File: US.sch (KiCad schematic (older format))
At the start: 1 part, among them J10 Conn_01x04

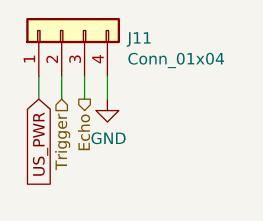
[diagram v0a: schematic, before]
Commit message: PCB routed, no errors but still a few tracks too close
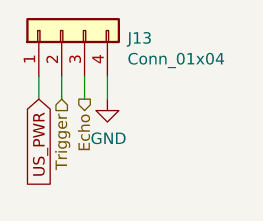
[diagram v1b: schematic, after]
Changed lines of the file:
@@
 AR Path="/5BC05284/5BC053B5" Ref="J12"  Part="1"
 AR Path="/5BC05291/5BC053B5" Ref="J13"  Part="1"
-F 0 "J11" V 3966 2262 50  0000 R CNN
+F 0 "J13" V 3966 2262 50  0000 R CNN
 F 1 "Conn_01x04" V 3875 2262 50  0000 R CNN
 F 2 "Connector_JST:JST_PH_B4B-PH-K_1x04_P2.00mm_Vertical" H 4000 2550 50  0001 C CNN
@@
 AR Path="/5BC05284/5BC072A4" Ref="#PWR053"  Part="1"
 AR Path="/5BC05291/5BC072A4" Ref="#PWR054"  Part="1"
-F 0 "#PWR052" H 4200 2600 50  0001 C CNN
+F 0 "#PWR054" H 4200 2600 50  0001 C CNN
 F 1 "GND" H 4205 2677 50  0000 C CNN
 F 2 "" H 4200 2850 50  0001 C CNN

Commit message: Corrected, routing redone
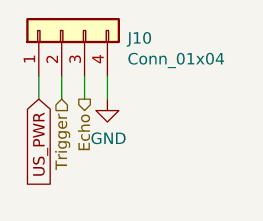
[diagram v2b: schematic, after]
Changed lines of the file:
@@
 $Descr A4 11693 8268
 encoding utf-8
-Sheet 12 19
+Sheet 15 19
 Title ""
 Date ""
@@
 AR Path="/5BC05284/5BC053B5" Ref="J12"  Part="1"
 AR Path="/5BC05291/5BC053B5" Ref="J13"  Part="1"
-F 0 "J13" V 3966 2262 50  0000 R CNN
+F 0 "J10" V 3966 2262 50  0000 R CNN
 F 1 "Conn_01x04" V 3875 2262 50  0000 R CNN
 F 2 "Connector_JST:JST_PH_B4B-PH-K_1x04_P2.00mm_Vertical" H 4000 2550 50  0001 C CNN
@@
 AR Path="/5BC05284/5BC072A4" Ref="#PWR053"  Part="1"
 AR Path="/5BC05291/5BC072A4" Ref="#PWR054"  Part="1"
-F 0 "#PWR054" H 4200 2600 50  0001 C CNN
+F 0 "#PWR051" H 4200 2600 50  0001 C CNN
 F 1 "GND" H 4205 2677 50  0000 C CNN
 F 2 "" H 4200 2850 50  0001 C CNN

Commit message: Added RS refs
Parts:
- J10: RS (none) -> 820-1434
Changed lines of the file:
@@
 F 2 "Connector_JST:JST_PH_B4B-PH-K_1x04_P2.00mm_Vertical" H 4000 2550 50  0001 C CNN
 F 3 "~" H 4000 2550 50  0001 C CNN
+F 4 "820-1434 " H 0   0   50  0001 C CNN "RS"
 	1    4000 2550
 	0    -1   -1   0
@@
 AR Path="/5BC05284/5BC072A4" Ref="#PWR053"  Part="1"
 AR Path="/5BC05291/5BC072A4" Ref="#PWR054"  Part="1"
-F 0 "#PWR051" H 4200 2600 50  0001 C CNN
+F 0 "#PWR054" H 4200 2600 50  0001 C CNN
 F 1 "GND" H 4205 2677 50  0000 C CNN
 F 2 "" H 4200 2850 50  0001 C CNN

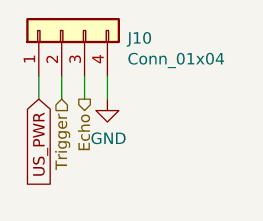
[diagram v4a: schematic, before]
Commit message: Rename phoenix phenix. Connect mounting holes to gnd.
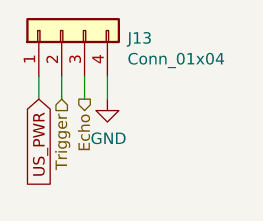
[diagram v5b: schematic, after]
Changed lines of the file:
@@
 EESchema Schematic File Version 4
+LIBS:ultraphotonicsense-elec-cache
 EELAYER 26 0
 EELAYER END
@@
 AR Path="/5BC05284/5BC053B5" Ref="J12"  Part="1"
 AR Path="/5BC05291/5BC053B5" Ref="J13"  Part="1"
-F 0 "J10" V 3966 2262 50  0000 R CNN
+F 0 "J13" V 3966 2262 50  0000 R CNN
 F 1 "Conn_01x04" V 3875 2262 50  0000 R CNN
 F 2 "Connector_JST:JST_PH_B4B-PH-K_1x04_P2.00mm_Vertical" H 4000 2550 50  0001 C CNN
